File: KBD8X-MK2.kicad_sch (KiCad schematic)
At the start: 22 parts, among them J1 AVR-ISP-6, Q1 DSS60601MZ4-13, SW1 SW_Push, U1 ATmega32U4-MU, U2 PRTR5V0U2X, Y1 16MHz

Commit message: Made the project portable
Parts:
- C2, C3, C4, C5, C6, C7, C8: footprint locallib:C_0603 -> KBD8X_MK2_Components:C_0603; symbol Device:C_Small -> KBD8X_MK2_Components:C_Small
- F1: footprint Fuse_Holders_and_Fuses:Fuse_SMD1206_Wave -> KBD8X_MK2_Components:Fuse_1206_3216Metric; symbol Device:Polyfuse_Small -> KBD8X_MK2_Components:Polyfuse_Small
- J1: footprint random-keyboard-parts:Reset_Pretty-Mask -> KBD8X_MK2_Components:Reset_Pretty-Mask; symbol Connector:AVR-ISP-6 -> KBD8X_MK2_Components:AVR-ISP-6
- Q1: footprint TO_SOT_Packages_SMD:SOT-223-3_TabPin2 -> KBD8X_MK2_Components:SOT-223-3_TabPin2; symbol Device:Q_NPN_BCE -> KBD8X_MK2_Components:Q_NPN_BCE
- RC1, RC2, RC3, RC4, RC5, RC6, RC7: footprint locallib:R_0603 -> KBD8X_MK2_Components:R_0603; symbol Device:R_Small -> KBD8X_MK2_Components:R_Small
- SW1: footprint random-keyboard-parts:SKQG-1155865 -> KBD8X_MK2_Components:SKQG-1155865
- U1: footprint locallib:QFN-44-1EP_7x7mm_Pitch0.5mm -> Package_DFN_QFN:QFN-44-1EP_7x7mm_P0.5mm_EP5.2x5.2mm; symbol MCU_Microchip_ATmega:ATmega32U4-MU -> KBD8X_MK2_Components:ATmega32U4-M
- U2: footprint locallib:SOT143B -> KBD8X_MK2_Components:SOT143B; symbol ai03-locallib:PRTR5V0U2X -> KBD8X_MK2_Components:PRTR5V0U2X
- USB1: footprint Type-C:HRO-TYPE-C-31-M-12-Assembly -> KBD8X_MK2_Components:HRO-TYPE-C-31-M-12-Assembly; symbol Type-C:HRO-TYPE-C-31-M-12 -> KBD8X_MK2_Components:HRO-TYPE-C-31-M-12
- Y1: footprint locallib:Crystal_SMD_3225-4pin_3.2x2.5mm -> KBD8X_MK2_Components:Crystal_SMD_3225-4pin_3.2x2.5mm; symbol Device:Crystal_GND24 -> KBD8X_MK2_Components:Crystal_GND24

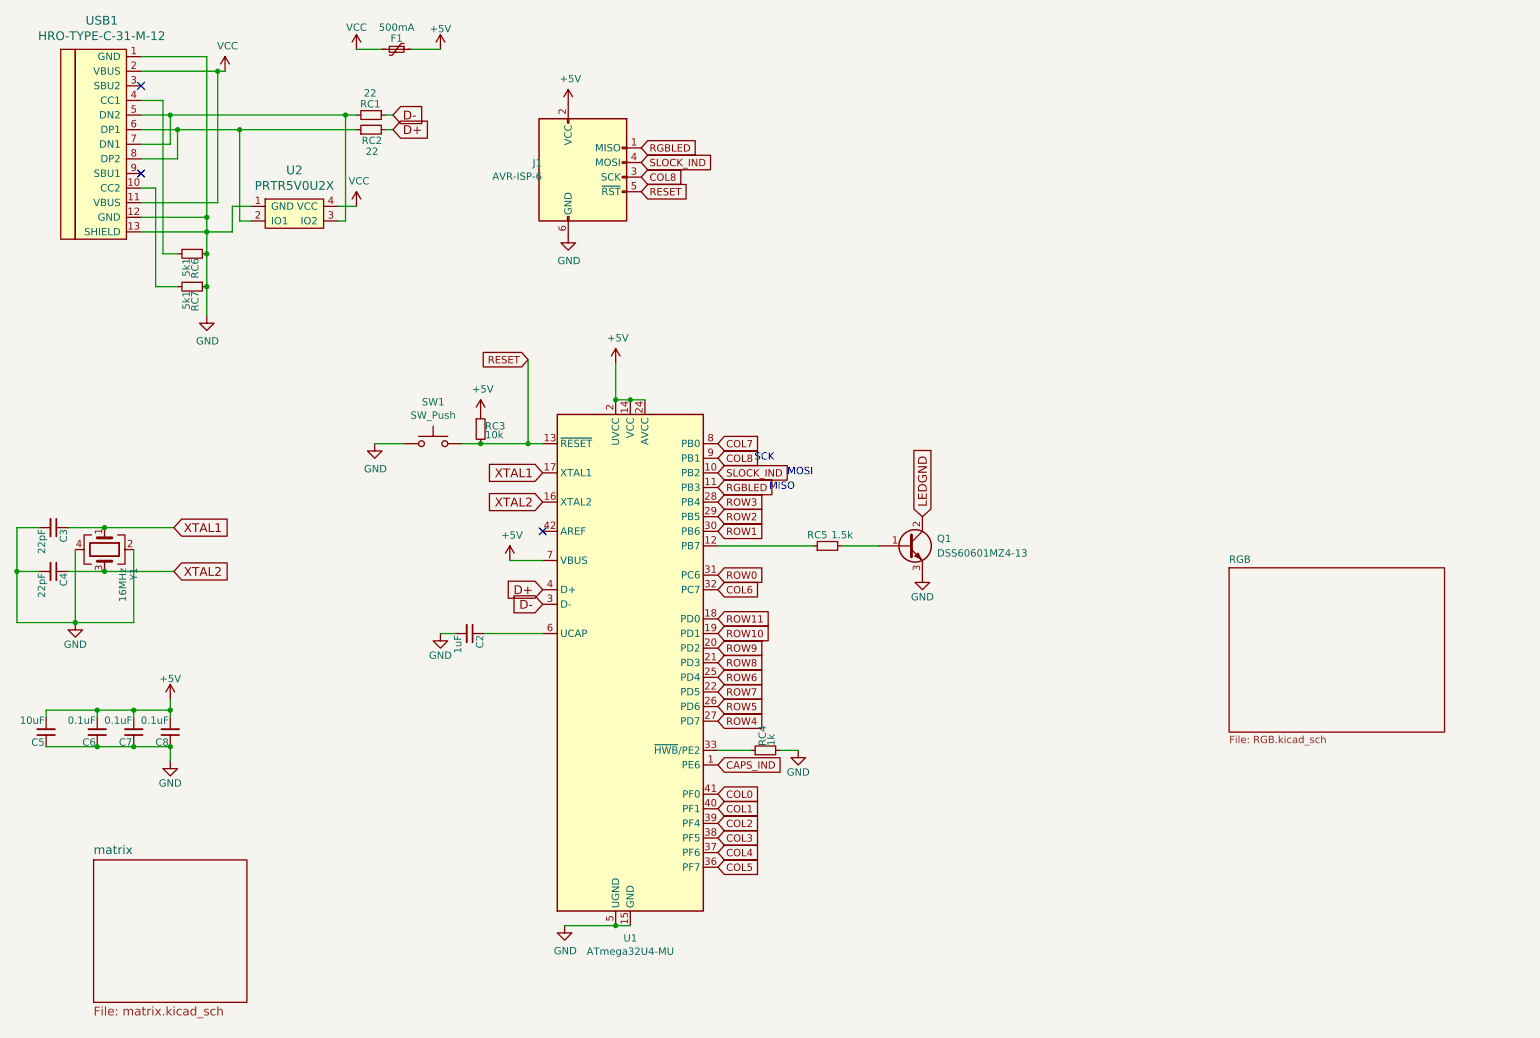
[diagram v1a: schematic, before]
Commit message: Rearrenged schematics items
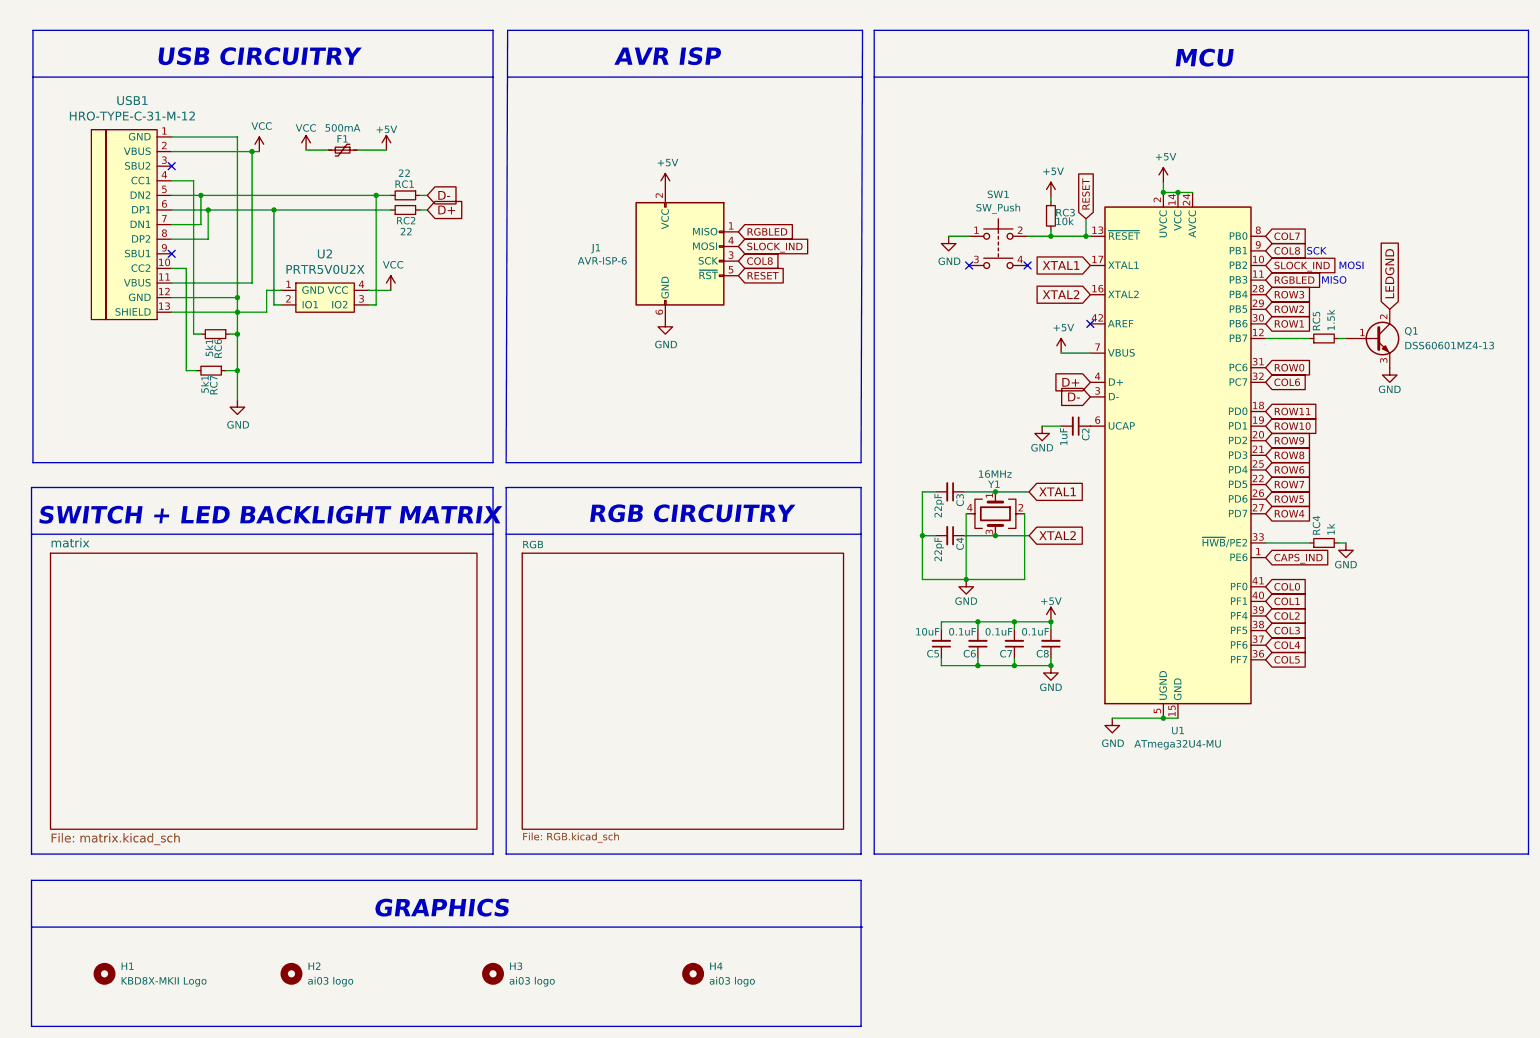
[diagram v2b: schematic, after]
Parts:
- added H1: KBD8X-MKII Logo, KBD8X_MK2_Graphics:kbd8x-logo, symbol Mechanical:MountingHole
- added H2: ai03 logo, KBD8X_MK2_Graphics:ai-ring-6mm-FancyAss, symbol Mechanical:MountingHole
- added H3: ai03 logo, KBD8X_MK2_Graphics:ai-ring-6mm-FancyAss-Mask, symbol Mechanical:MountingHole
- added H4: ai03 logo, KBD8X_MK2_Graphics:ai-ring-6mm, symbol Mechanical:MountingHole
- SW1: symbol Switch:SW_Push -> Switch:SW_Push_Dual
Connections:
- no-connect marks 3 -> 5
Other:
- note added: "AVR ISP"
- note added: "GRAPHICS"
- note added: "MCU"
- note added: "RGB CIRCUITRY"
- note added: "SWITCH + LED BACKLIGHT MATRIX"
- note added: "USB CIRCUITRY"
- moved on the sheet: C2, C3, C4, C5, C6, C7, C8, F1, J1, Q1, RC1, RC2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

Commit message: Updated symbols used in the schematics
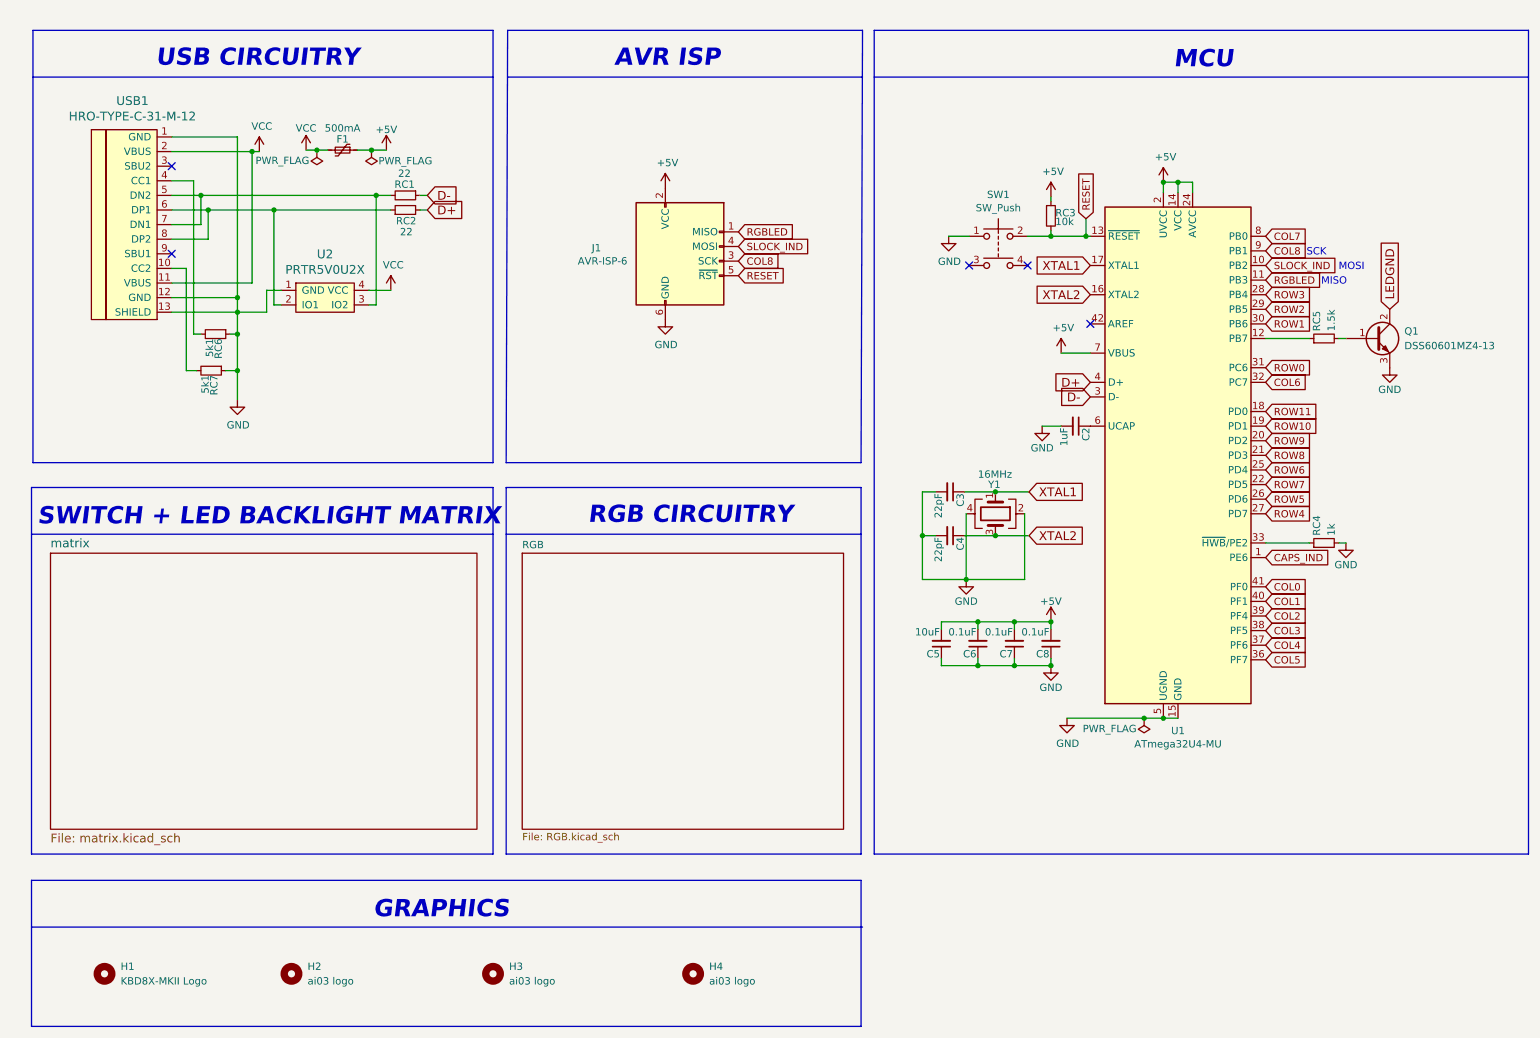
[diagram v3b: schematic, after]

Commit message: Added 3U and 10U footprints to the PCB
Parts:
- U1: footprint Package_DFN_QFN:QFN-44-1EP_7x7mm_P0.5mm_EP5.2x5.2mm -> KBD8X_MK2_Components:QFN-44-1EP_7x7mm_Pitch0.5mm
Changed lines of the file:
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@@
     (property "Reference" "U1" (id 0) (at 217.17 140.1064 0))
     (property "Value" "ATmega32U4-MU" (id 1) (at 217.17 142.4178 0))
-    (property "Footprint" "Package_DFN_QFN:QFN-44-1EP_7x7mm_P0.5mm_EP5.2x5.2mm" (id 2) (at 217.17 92.202 0)
+    (property "Footprint" "KBD8X_MK2_Components:QFN-44-1EP_7x7mm_Pitch0.5mm" (id 2) (at 217.17 92.202 0)
       (effects (font (size 1.27 1.27) italic) hide)
     )
@@
       (reference "D14") (unit 1) (value "SOD-123") (footprint "KBD8X_MK2_Components:D_SOD-123")
     )
+    (path "/00000000-0000-0000-0000-00005a286589/bab302bc-7e19-4757-8b90-b56e0a741d17"
+      (reference "D15") (unit 1) (value "SOD-123") (footprint "KBD8X_MK2_Components:D_SOD-123")
+    )
+    (path "/00000000-0000-0000-0000-00005a286589/1b67fb45-967f-4677-b5e7-3629e5c7e3cf"
+      (reference "D16") (unit 1) (value "SOD-123") (footprint "KBD8X_MK2_Components:D_SOD-123")
+    )
     (path "/00000000-0000-0000-0000-00005a286589/00000000-0000-0000-0000-00005a2e3fb7"
       (reference "D17") (unit 1) (value "SOD-123") (footprint "KBD8X_MK2_Components:D_SOD-123")
@@
       (reference "MX_SP2") (unit 1) (value "MX-LED") (footprint "KBD8X_MK2_Switches:MXOnly-7U-ReversedStabilizers")
     )
+    (path "/00000000-0000-0000-0000-00005a286589/ff19663e-6654-48a3-9e52-2b7991658e2f"
+      (reference "MX_SP3") (unit 1) (value "MX-LED") (footprint "KBD8X_MK2_Switches:MXOnly-10U-ReversedStabilizers")
+    )
+    (path "/00000000-0000-0000-0000-00005a286589/dd80a9f5-5787-4151-8a40-e3db0bb644de"
+      (reference "MX_SP4") (unit 1) (value "MX-LED") (footprint "KBD8X_MK2_Switches:MXOnly-1U")
+    )
+    (path "/00000000-0000-0000-0000-00005a286589/c3c0243c-11eb-4307-8b03-c34e380759d2"
+      (reference "MX_SSPC1") (unit 1) (value "MX-LED") (footprint "KBD8X_MK2_Switches:MXOnly-3U-ReversedStabilizers")
+    )
+    (path "/00000000-0000-0000-0000-00005a286589/69946e69-8fe4-48a5-b7d1-ca6775e4099a"
+      (reference "MX_SSPC2") (unit 1) (value "MX-LED") (footprint "KBD8X_MK2_Switches:MXOnly-3U-ReversedStabilizers")
+    )
     (path "/00000000-0000-0000-0000-00005a286589/00000000-0000-0000-0000-00005a2ed3b1"
       (reference "MX_T1") (unit 1) (value "MX-LED") (footprint "KBD8X_MK2_Switches:MXOnly-1U")
@@
       (reference "R14") (unit 1) (value "1k") (footprint "KBD8X_MK2_Components:R_0603")
     )
+    (path "/00000000-0000-0000-0000-00005a286589/bbcc330a-fe9f-4945-92a4-73ed1cf6023e"
+      (reference "R15") (unit 1) (value "1k") (footprint "KBD8X_MK2_Components:R_0603")
+    )
     (path "/00000000-0000-0000-0000-00005a286589/00000000-0000-0000-0000-00006421446e"
       (reference "R16") (unit 1) (value "1k") (footprint "KBD8X_MK2_Components:R_0603")
@@
       (reference "R33") (unit 1) (value "1k") (footprint "KBD8X_MK2_Components:R_0603")
     )
+    (path "/00000000-0000-0000-0000-00005a286589/78647be1-71ed-4476-be12-28adaa8c6f31"
+      (reference "R34") (unit 1) (value "1k") (footprint "KBD8X_MK2_Components:R_0603")
+    )
     (path "/00000000-0000-0000-0000-00005a286589/00000000-0000-0000-0000-00005a2ed33f"
       (reference "R35") (unit 1) (value "1k") (footprint "KBD8X_MK2_Components:R_0603")
@@
     )
     (path "/00000000-0000-0000-0000-00005c8a33e3/00000000-0000-0000-0000-00005c8a54fd"
-      (reference "RGB1") (unit 1) (value "WS2812B") (footprint "LED_SMD:LED_WS2812B_PLCC4_5.0x5.0mm_P3.2mm")
+      (reference "RGB1") (unit 1) (value "WS2812B") (footprint "KBD8X_MK2_Components:LED_WS2812B-PLCC4")
     )
     (path "/00000000-0000-0000-0000-00005c8a33e3/00000000-0000-0000-0000-00005c8a5510"
-      (reference "RGB2") (unit 1) (value "WS2812B") (footprint "LED_SMD:LED_WS2812B_PLCC4_5.0x5.0mm_P3.2mm")
+      (reference "RGB2") (unit 1) (value "WS2812B") (footprint "KBD8X_MK2_Components:LED_WS2812B-PLCC4")
     )
     (path "/00000000-0000-0000-0000-00005c8a33e3/00000000-0000-0000-0000-00005c8a5523"
-      (reference "RGB3") (unit 1) (value "WS2812B") (footprint "LED_SMD:LED_WS2812B_PLCC4_5.0x5.0mm_P3.2mm")
+      (reference "RGB3") (unit 1) (value "WS2812B") (footprint "KBD8X_MK2_Components:LED_WS2812B-PLCC4")
     )
     (path "/00000000-0000-0000-0000-00005c8a33e3/00000000-0000-0000-0000-00005c8a5536"
-      (reference "RGB4") (unit 1) (value "WS2812B") (footprint "LED_SMD:LED_WS2812B_PLCC4_5.0x5.0mm_P3.2mm")
+      (reference "RGB4") (unit 1) (value "WS2812B") (footprint "KBD8X_MK2_Components:LED_WS2812B-PLCC4")
     )
     (path "/00000000-0000-0000-0000-00005c8a33e3/00000000-0000-0000-0000-00005c8a9518"
-      (reference "RGB5") (unit 1) (value "WS2812B") (footprint "LED_SMD:LED_WS2812B_PLCC4_5.0x5.0mm_P3.2mm")
+      (reference "RGB5") (unit 1) (value "WS2812B") (footprint "KBD8X_MK2_Components:LED_WS2812B-PLCC4")
     )
     (path "/00000000-0000-0000-0000-00005c8a33e3/00000000-0000-0000-0000-00005c8a952b"
-      (reference "RGB6") (unit 1) (value "WS2812B") (footprint "LED_SMD:LED_WS2812B_PLCC4_5.0x5.0mm_P3.2mm")
+      (reference "RGB6") (unit 1) (value "WS2812B") (footprint "KBD8X_MK2_Components:LED_WS2812B-PLCC4")
     )
     (path "/00000000-0000-0000-0000-00005c8a33e3/00000000-0000-0000-0000-00005c8a953e"
-      (reference "RGB7") (unit 1) (value "WS2812B") (footprint "LED_SMD:LED_WS2812B_PLCC4_5.0x5.0mm_P3.2mm")
+      (reference "RGB7") (unit 1) (value "WS2812B") (footprint "KBD8X_MK2_Components:LED_WS2812B-PLCC4")
     )
     (path "/00000000-0000-0000-0000-00005c8a33e3/00000000-0000-0000-0000-00005c8a9551"
-      (reference "RGB8") (unit 1) (value "WS2812B") (footprint "LED_SMD:LED_WS2812B_PLCC4_5.0x5.0mm_P3.2mm")
+      (reference "RGB8") (unit 1) (value "WS2812B") (footprint "KBD8X_MK2_Components:LED_WS2812B-PLCC4")
     )
     (path "/00000000-0000-0000-0000-00005c8a33e3/00000000-0000-0000-0000-00005c8a9c20"
-      (reference "RGB9") (unit 1) (value "WS2812B") (footprint "LED_SMD:LED_WS2812B_PLCC4_5.0x5.0mm_P3.2mm")
+      (reference "RGB9") (unit 1) (value "WS2812B") (footprint "KBD8X_MK2_Components:LED_WS2812B-PLCC4")
     )
     (path "/00000000-0000-0000-0000-00005c8a33e3/00000000-0000-0000-0000-00005c8a9c33"
-      (reference "RGB10") (unit 1) (value "WS2812B") (footprint "LED_SMD:LED_WS2812B_PLCC4_5.0x5.0mm_P3.2mm")
+      (reference "RGB10") (unit 1) (value "WS2812B") (footprint "KBD8X_MK2_Components:LED_WS2812B-PLCC4")
     )
     (path "/00000000-0000-0000-0000-00005c8a33e3/00000000-0000-0000-0000-00005c8a9c46"
-      (reference "RGB11") (unit 1) (value "WS2812B") (footprint "LED_SMD:LED_WS2812B_PLCC4_5.0x5.0mm_P3.2mm")
+      (reference "RGB11") (unit 1) (value "WS2812B") (footprint "KBD8X_MK2_Components:LED_WS2812B-PLCC4")
     )
     (path "/00000000-0000-0000-0000-00005c8a33e3/00000000-0000-0000-0000-00005c8a9c59"
-      (reference "RGB12") (unit 1) (value "WS2812B") (footprint "LED_SMD:LED_WS2812B_PLCC4_5.0x5.0mm_P3.2mm")
+      (reference "RGB12") (unit 1) (value "WS2812B") (footprint "KBD8X_MK2_Components:LED_WS2812B-PLCC4")
     )
     (path "/00000000-0000-0000-0000-00005c8a33e3/00000000-0000-0000-0000-00005c8a9c75"
-      (reference "RGB13") (unit 1) (value "WS2812B") (footprint "LED_SMD:LED_WS2812B_PLCC4_5.0x5.0mm_P3.2mm")
+      (reference "RGB13") (unit 1) (value "WS2812B") (footprint "KBD8X_MK2_Components:LED_WS2812B-PLCC4")
     )
     (path "/00000000-0000-0000-0000-00005c8a33e3/00000000-0000-0000-0000-00005c8a9c88"
-      (reference "RGB14") (unit 1) (value "WS2812B") (footprint "LED_SMD:LED_WS2812B_PLCC4_5.0x5.0mm_P3.2mm")
+      (reference "RGB14") (unit 1) (value "WS2812B") (footprint "KBD8X_MK2_Components:LED_WS2812B-PLCC4")
     )
     (path "/00000000-0000-0000-0000-00005c8a33e3/00000000-0000-0000-0000-00005c8a9c9b"
-      (reference "RGB15") (unit 1) (value "WS2812B") (footprint "LED_SMD:LED_WS2812B_PLCC4_5.0x5.0mm_P3.2mm")
+      (reference "RGB15") (unit 1) (value "WS2812B") (footprint "KBD8X_MK2_Components:LED_WS2812B-PLCC4")
     )
     (path "/00000000-0000-0000-0000-00005c8a33e3/00000000-0000-0000-0000-00005c8a9cae"
-      (reference "RGB16") (unit 1) (value "WS2812B") (footprint "LED_SMD:LED_WS2812B_PLCC4_5.0x5.0mm_P3.2mm")
+      (reference "RGB16") (unit 1) (value "WS2812B") (footprint "KBD8X_MK2_Components:LED_WS2812B-PLCC4")
     )
     (path "/00000000-0000-0000-0000-00005c8a33e3/00000000-0000-0000-0000-00005c8aa4bc"
-      (reference "RGB17") (unit 1) (value "WS2812B") (footprint "LED_SMD:LED_WS2812B_PLCC4_5.0x5.0mm_P3.2mm")
+      (reference "RGB17") (unit 1) (value "WS2812B") (footprint "KBD8X_MK2_Components:LED_WS2812B-PLCC4")
     )
     (path "/00000000-0000-0000-0000-00005c8a33e3/00000000-0000-0000-0000-00005c8aa4cf"
-      (reference "RGB18") (unit 1) (value "WS2812B") (footprint "LED_SMD:LED_WS2812B_PLCC4_5.0x5.0mm_P3.2mm")
+      (reference "RGB18") (unit 1) (value "WS2812B") (footprint "KBD8X_MK2_Components:LED_WS2812B-PLCC4")
     )
     (path "/00000000-0000-0000-0000-00005c4db62b"
@@
     )
     (path "/00000000-0000-0000-0000-0000618b6d6d"
-      (reference "U1") (unit 1) (value "ATmega32U4-MU") (footprint "Package_DFN_QFN:QFN-44-1EP_7x7mm_P0.5mm_EP5.2x5.2mm")
+      (reference "U1") (unit 1) (value "ATmega32U4-MU") (footprint "KBD8X_MK2_Components:QFN-44-1EP_7x7mm_Pitch0.5mm")
     )
     (path "/00000000-0000-0000-0000-00005be1fa08"
